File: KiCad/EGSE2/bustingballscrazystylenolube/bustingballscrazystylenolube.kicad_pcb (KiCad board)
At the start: 4 copper layers, 70 parts, among them J1 USB_C_Receptacle_USB2.0_16P, J2 USB_C_Receptacle_USB2.0_16P, J3 DA15_Socket_MountingHoles, Q1 SIS412DN-T1-GE3, Q2 SIS412DN-T1-GE3, Q3 SIS412DN-T1-GE3, Q4 SIS412DN-T1-GE3, U1 TPS25730DREFR, U2 TLV76033DBZR, U3 BQ25713BRSNR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

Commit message: shaboining
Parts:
- R16: footprint Resistor_SMD:R_0805_2012Metric_Pad1.20x1.40mm_HandSolder -> Resistor_SMD:R_2512_6332Metric_Pad1.40x3.35mm_HandSolder
- moved U3 167.2 mm to (54.1, -45.8), turned to 90 degrees
- moved R18 156.1 mm to (42.0, -52.6), turned to 90 degrees
- moved R16 154.6 mm to (40.8, -57.0)
- moved R17 152.9 mm to (39.5, -52.6), turned to 90 degrees
- moved Q3 151.2 mm to (60.0, -57.0)
- moved Q4 147.6 mm to (56.1, -53.1), turned to 90 degrees
- moved C16 144.8 mm to (59.5, -52.1), turned to -90 degrees
- moved Q2 142.0 mm to (51.9, -53.1), turned to 90 degrees
- moved Q1 138.1 mm to (48.0, -57.0), turned to 180 degrees
- moved L1 137.5 mm to (54.0, -58.6)
- moved C15 133.5 mm to (48.5, -52.1), turned to -90 degrees
- moved R1 73.3 mm to (13.7, -39.1), turned to -90 degrees
- moved R3 69.4 mm to (11.2, -39.1), turned to -90 degrees
- moved R2 67.7 mm to (8.76, -39.1), turned to -90 degrees
- moved C3 67.5 mm to (16.8, -45.5), turned to -90 degrees
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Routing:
- net /USBHELL/Reserved_26: track 0.00 -> 20.8 mm, vias 0 -> 2
- net /IO/CC2: track 3.56 -> 22.0 mm, vias 0 -> 2
- net /BttChg/HIDRV1: track 0.00 -> 17.4 mm, vias 0 -> 2
- net /USBHELL/Reserved_27: track 0.00 -> 17.3 mm, vias 0 -> 2
- net /IO/CC1: track 5.79 -> 22.3 mm, vias 0 -> 2
- net /USBHELL/PLUG_FLIP: track 0.00 -> 16.5 mm, vias 0 -> 2
- net /BttChg/HIDRV2: track 0.00 -> 12.9 mm, vias 0 -> 2
- net /USBHELL/Reserved_36: track 0.00 -> 12.0 mm, vias 0 -> 2
- net /BttChg/REGN: track 0.00 -> 11.7 mm, vias 0 -> 1
- net /BttChg/SW1: track 0.00 -> 11.0 mm
- net /BttChg/SW2: track 0.00 -> 9.78 mm
- net /IO/VBUS: track 0.00 -> 8.91 mm, vias 0 -> 2
- net /USBHELL/3V3_LED: track 0.00 -> 8.82 mm
- net /USBHELL/PLUG_EVENT: track 0.00 -> 7.20 mm
- net /BttChg/BTST1: track 0.00 -> 7.08 mm
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- added copper zone on F.Cu, net /BttChg/IN
- added copper zone on F.Cu, net /BttChg/PPHV
- added copper zone on F.Cu, net /BttChg/SW1
- added copper zone on F.Cu, net /BttChg/SW2
- added copper zone on F.Cu, net /IO/VBUS
- added copper zone on F.Cu, net GND

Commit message: slumpt
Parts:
- added H1: MountingHole, MountingHole:MountingHole_3mm_Pad, F.Cu at (109.2, 72.4)
- added H2: MountingHole, MountingHole:MountingHole_3mm_Pad, F.Cu at (195.6, 72.4)
- added H3: MountingHole, MountingHole:MountingHole_3mm_Pad, F.Cu at (109.2, 138.4)
- added H4: MountingHole, MountingHole:MountingHole_3mm_Pad, F.Cu at (195.6, 138.6)
- added IN1: IN, TestPoint:TestPoint_Pad_1.0x1.0mm, F.Cu at (149.0, 82.9)
- added J4: Conn_02x08_Top_Bottom, Connector_PinHeader_2.54mm:PinHeader_2x08_P2.54mm_Vertical, F.Cu at (181.7, 100.5)
- added OUT1: OUT, TestPoint:TestPoint_Pad_1.0x1.0mm, F.Cu at (169.4, 82.4)
- added PPHV1: PPHV, TestPoint:TestPoint_Pad_1.0x1.0mm, F.Cu at (132.7, 83.6)
- added SW1: SW1, TestPoint:TestPoint_Pad_1.0x1.0mm, F.Cu at (154.5, 82.0)
- added SW2: SW2, TestPoint:TestPoint_Pad_1.0x1.0mm, F.Cu at (163.9, 82.0)
- added VBATT1: VBATT, TestPoint:TestPoint_Pad_1.0x1.0mm, F.Cu at (179.8, 86.0)
- added VDDA1: VDDA, TestPoint:TestPoint_Pad_1.0x1.0mm, F.Cu at (154.0, 101.3)
- R22: footprint Resistor_SMD:R_0805_2012Metric_Pad1.20x1.40mm_HandSolder -> Resistor_SMD:R_2512_6332Metric_Pad1.40x3.35mm_HandSolder
- moved J3 346.1 mm to (193.2, 103.9), turned to 90 degrees
- moved C12 326.2 mm to (182.6, 96.7), turned to 180 degrees
- moved C13 324.0 mm to (182.6, 93.6), turned to 180 degrees
- moved C8 323.5 mm to (182.6, 90.5), turned to 180 degrees
- moved C21 310.9 mm to (169.1, 103.7)
- moved C18 310.2 mm to (172.4, 90.3)
- moved C22 308.7 mm to (167.0, 105.9)
- moved C17 308.3 mm to (169.1, 91.2), turned to -90 degrees
- moved C24 306.5 mm to (169.1, 101.6)
- moved C23 304.9 mm to (167.0, 99.4)
- moved R21 302.5 mm to (173.8, 93.7), turned to 90 degrees
- moved R20 301.2 mm to (171.1, 93.7), turned to 90 degrees
- moved C6 298.5 mm to (149.6, 92.4), turned to -90 degrees
- moved R22 297.3 mm to (172.4, 86.0)
- moved C19 297.0 mm to (154.0, 104.5), turned to -90 degrees
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- renumbered C8 to C11, C11 to C8
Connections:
- C12 pad 1: /BttChg/PPHV -> /BttChg/VBATT
- C13 pad 1: /BttChg/PPHV -> /BttChg/VBATT
- C8 pad 1: /BttChg/PPHV -> /BttChg/VBATT
- J3 pad 10: /BttChg/VBATT -> unconnected-(J3-P10-Pad10)
- J3 pad 13: unconnected-(J3-P13-Pad13) -> GND
- J3 pad 15: /CP2102/RXD -> unconnected-(J3-P15-Pad15)
- J3 pad 3: GND -> /BttChg/VBATT
- J3 pad 4: GND -> /CP2102/TXD
- J3 pad 5: unconnected-(J3-Pad5) -> /CP2102/RXD
- J3 pad 6: unconnected-(J3-Pad6) -> /BttChg/VBATT
- J3 pad 7: unconnected-(J3-Pad7) -> /BttChg/VBATT
- J3 pad 8: /CP2102/TXD -> GND
- J3 pad 9: /BttChg/VBATT -> GND
- Q3 pad 5: /BttChg/VBATT -> /BttChg/OUT
- Q3 pad 6: /BttChg/VBATT -> /BttChg/OUT
- Q3 pad 7: /BttChg/VBATT -> /BttChg/OUT
- Q3 pad 8: /BttChg/VBATT -> /BttChg/OUT
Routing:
- net GND: track 1.81 -> 82.7 mm, vias 4 -> 24
- net /CP2102/TXD: track 0.00 -> 76.4 mm
- net /CP2102/RXD: track 0.00 -> 74.5 mm
- net /BttChg/I2Ct_SCL: track 4.91 -> 55.8 mm
- net /BttChg/I2Ct_SDA: track 5.57 -> 54.2 mm
- net /BttChg/OUT: track 2.49 -> 27.1 mm
- net /CP2102/VBUS_comm: track 0.00 -> 22.5 mm
- net /BttChg/V_CHG: track 0.91 -> 20.1 mm
- net Net-(U3-ACP): track 0.91 -> 19.2 mm, vias 0 -> 2
- net Net-(U3-ACN): track 0.91 -> 16.2 mm, vias 0 -> 2
- net /BttChg/REGN: track 11.7 -> 25.5 mm, vias 1 -> 2
- net Net-(U4-VDD): track 0.00 -> 13.6 mm, vias 0 -> 2
- net Net-(U3-SRN): track 0.91 -> 13.8 mm
- net /CP2102/D+: track 0.00 -> 11.9 mm
- net /CP2102/D-: track 0.00 -> 11.9 mm
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- added copper zone on F.Cu, net /BttChg/OUT
- added copper zone on F.Cu, net /BttChg/VBATT
- added copper zone on B.Cu, net GND
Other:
- board outline added: 101.6 x 81.3 mm
- copper layers 4 -> 2

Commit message: done
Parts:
- added G***: LOGO, LOGO, F.Cu at (154.2, 127.1)
- added G***: LOGO, LOGO, B.Cu at (129.2, 82.9)
- added G***: LOGO, LOGO, B.Cu at (128.5, 139.5)
- added G***: LOGO, LOGO, B.Cu at (166.3, 73.8)
- added G***: LOGO, LOGO, B.Cu at (164.8, 131.0)

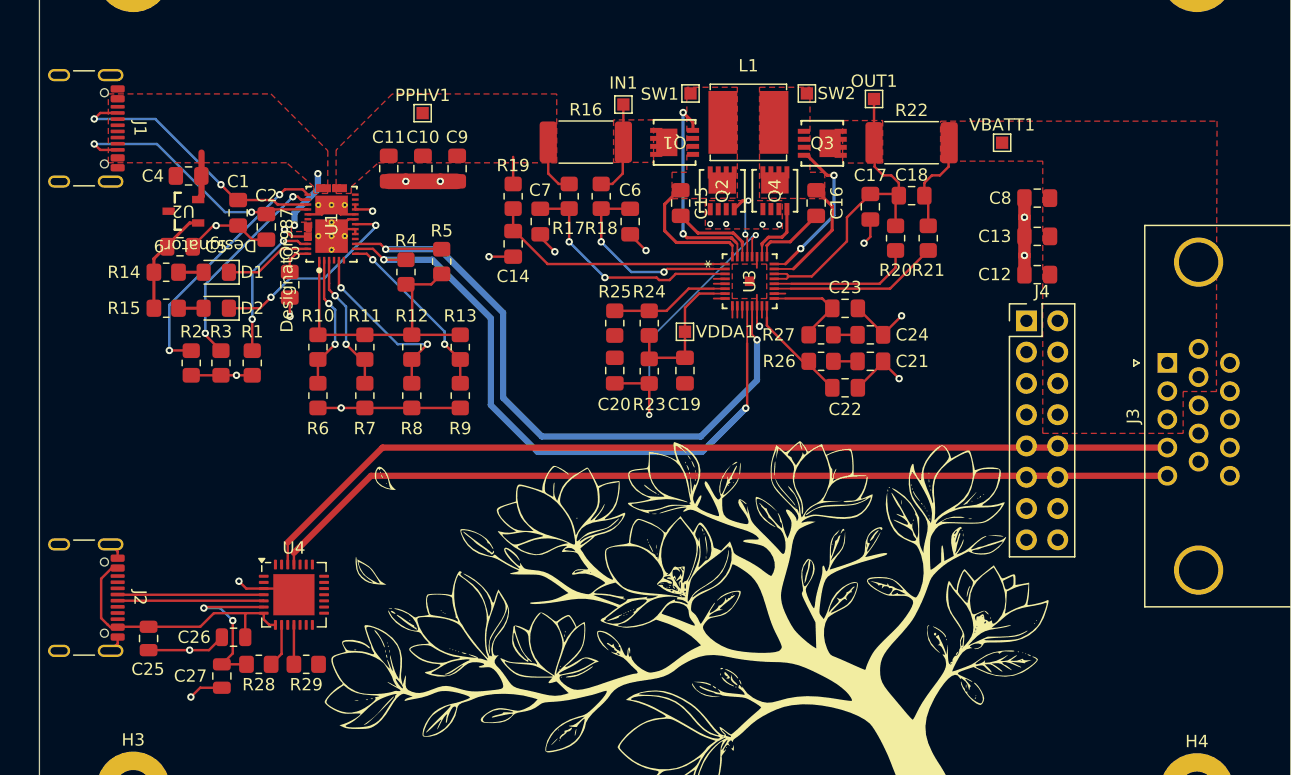
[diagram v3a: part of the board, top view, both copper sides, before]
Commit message: added more copper on pwr path
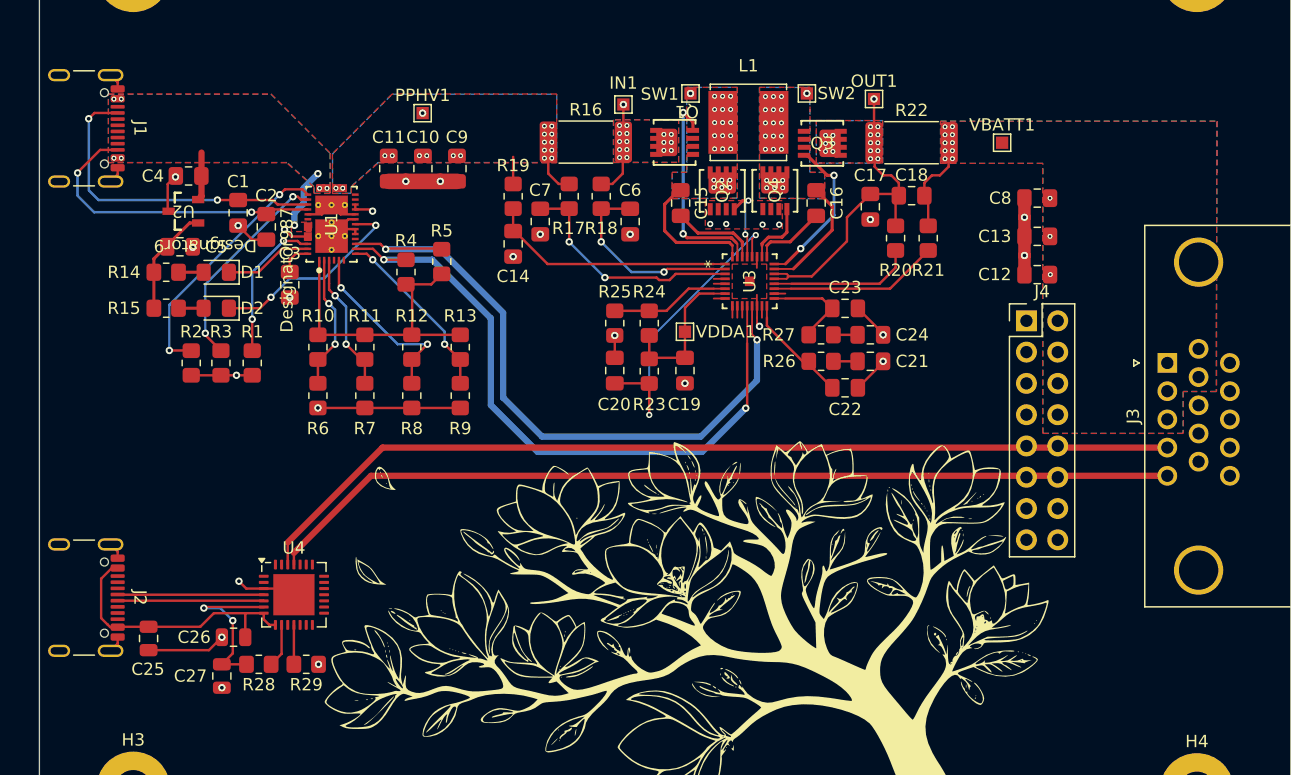
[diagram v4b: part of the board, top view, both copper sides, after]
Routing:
- net GND: track 82.7 -> 69.7 mm, vias 24 -> 29
- net /IO/CC1: track 22.3 -> 26.6 mm
- net /IO/CC2: track 22.0 -> 25.4 mm
- net /IO/VBUS: vias 2 -> 8
- net /BttChg/VBATT: vias 0 -> 13
- net /BttChg/SW2: vias 0 -> 22
- net /BttChg/SW1: vias 0 -> 22
- net /BttChg/PPHV: vias 0 -> 19
- net /BttChg/OUT: vias 0 -> 17
- net /BttChg/IN: vias 0 -> 17
- added copper zone on B.Cu, net /BttChg/IN
- added copper zone on B.Cu, net /BttChg/OUT
- added copper zone on B.Cu, net /BttChg/PPHV
- added copper zone on B.Cu, net /BttChg/SW1
- added copper zone on B.Cu, net /BttChg/SW2
- added copper zone on B.Cu, net /BttChg/VBATT
- added copper zone on B.Cu, net /IO/VBUS

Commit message: shmovwe
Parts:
- added J5: Conn_01x03_Pin, Connector_PinHeader_2.54mm:PinHeader_1x03_P2.54mm_Vertical, F.Cu at (143.7, 102.0)
- added R30: 60k, Resistor_SMD:R_0805_2012Metric_Pad1.20x1.40mm_HandSolder, F.Cu at (156.5, 102.5)
- added R31: 40k, Resistor_SMD:R_0805_2012Metric_Pad1.20x1.40mm_HandSolder, F.Cu at (156.5, 106.5)
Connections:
- Q1 pad 9: /BttChg/IN -> (no net)
- Q2 pad 9: /BttChg/SW1 -> (no net)
- Q3 pad 9: /BttChg/OUT -> (no net)
- Q4 pad 9: /BttChg/SW2 -> (no net)
- U3 pad 21: /BttChg/OUT -> unconnected-(U3-*BATDRV-Pad21)
- U3 pad 5: /BttChg/OTG/VAP -> GND
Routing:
- net /BttChg/CELL_BATPRESZ: track 0.91 -> 15.2 mm, vias 0 -> 2
- net GND: track 69.7 -> 73.8 mm, vias 29 -> 30
- net /BttChg/VDDA: track 12.6 -> 15.2 mm
- net /BttChg/I2Ct_SDA: track 54.2 -> 52.6 mm
- net /BttChg/I2Ct_SCL: track 55.8 -> 54.2 mm
- net /BttChg/OUT: track 27.1 -> 25.8 mm
- net /BttChg/OTG/VAP: track 0.91 -> 0.00 mm
